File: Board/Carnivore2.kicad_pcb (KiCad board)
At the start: 2 copper layers, 99 x 65.6 mm, 135 parts, among them J1 Conn_01x02_Pin, J2 Conn_01x03_Pin, U1 EP2C8Q208C8N, U2 MX29LV640ETTI-70G, U3 RMLV1616AGSA-5S#KA0, U4 M25P80-VMN3TPB, U5 PCM5101APWR, U6 AT93C46DN-SH-T, U7 SG3225CAN 50.0000M-TJGA6, U9 PCM1808PWR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

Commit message: Corrections in silkscreen for wrong direction of some capacitors and all diodes
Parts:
- moved D4 7.66 mm to (188.4, 113.4), turned to 180 degrees
- moved D1 7.63 mm to (191.6, 82.2), turned to 180 degrees
- moved D2 7.60 mm to (191.7, 86.8), turned to -90 degrees
- moved D3 7.59 mm to (178.0, 113.4), turned to 180 degrees
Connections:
- D1 pad 1: /VCC3.3 -> Net-(D1-K)
- D1 pad 2: Net-(D1-K) -> /VCC3.3
- D2 pad 1: Net-(D2-A) -> Net-(D1-K)
- D2 pad 2: Net-(D1-K) -> Net-(D2-A)
- D3 pad 1: /VCC3.3 -> Net-(D3-K)
- D3 pad 2: Net-(D3-K) -> /VCC3.3
- D4 pad 1: Net-(D3-K) -> Net-(D4-K)
- D4 pad 2: Net-(D4-K) -> Net-(D3-K)
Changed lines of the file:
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@@
   )
   (footprint "Diode_THT:D_DO-35_SOD27_P7.62mm_Horizontal" (layer "F.Cu")
-    (at 183.98 82.22)
+    (at 191.61 82.22 180)
     (descr "Diode, DO-35_SOD27 series, Axial, Horizontal, pin pitch=7.62mm, , length*diameter=4*2mm^2, , http://www.diodes.com/_files/packages/DO-35.pdf")
     (tags "Diode DO-35_SOD27 series Axial Horizontal pin pitch 7.62mm  length 4mm diameter 2mm")
@@
     (property "Sheetfile" "Carnivore2.kicad_sch")
     (property "Sheetname" "")
-    (property "ki_description" "Default Diode")
+    (property "Sim.Device" "D")
+    (property "Sim.Pins" "1=K 2=A")
+    (property "ki_description" "100V 0.15A standard switching diode, DO-35")
+    (property "ki_keywords" "diode")
     (attr through_hole)
     (fp_text reference "D1" (at 4.07 0) (layer "F.SilkS")
@@
     (fp_line (start 7.62 0) (end 5.81 0)
       (stroke (width 0.1) (type solid)) (layer "F.Fab"))
-    (pad "1" thru_hole rect (at 0 0) (size 1.6 1.6) (drill 0.8) (layers "*.Cu" "*.Mask")
-      (net 4 "/VCC3.3") (pinfunction "A") (pintype "passive"))
-    (pad "2" thru_hole oval (at 7.62 0) (size 1.6 1.6) (drill 0.8) (layers "*.Cu" "*.Mask")
+    (pad "1" thru_hole rect (at 0 0 180) (size 1.6 1.6) (drill 0.8) (layers "*.Cu" "*.Mask")
       (net 7 "Net-(D1-K)") (pinfunction "K") (pintype "passive"))
+    (pad "2" thru_hole oval (at 7.62 0 180) (size 1.6 1.6) (drill 0.8) (layers "*.Cu" "*.Mask")
+      (net 4 "/VCC3.3") (pinfunction "A") (pintype "passive"))
     (model "${KICAD6_3DMODEL_DIR}/Diode_THT.3dshapes/D_DO-35_SOD27_P7.62mm_Horizontal.wrl"
       (offset (xyz 0 0 0))
@@
   )
   (footprint "Diode_THT:D_DO-35_SOD27_P7.62mm_Horizontal" (layer "F.Cu")
-    (at 191.65 94.37 90)
+    (at 191.65 86.77 -90)
     (descr "Diode, DO-35_SOD27 series, Axial, Horizontal, pin pitch=7.62mm, , length*diameter=4*2mm^2, , http://www.diodes.com/_files/packages/DO-35.pdf")
     (tags "Diode DO-35_SOD27 series Axial Horizontal pin pitch 7.62mm  length 4mm diameter 2mm")
@@
     (property "Sheetfile" "Carnivore2.kicad_sch")
     (property "Sheetname" "")
-    (property "ki_description" "Default Diode")
+    (property "Sim.Device" "D")
+    (property "Sim.Pins" "1=K 2=A")
+    (property "ki_description" "100V 0.15A standard switching diode, DO-35")
+    (property "ki_keywords" "diode")
     (attr through_hole)
     (fp_text reference "D2" (at 3.95 0.05 90) (layer "F.SilkS")
@@
     (fp_line (start 7.62 0) (end 5.81 0)
       (stroke (width 0.1) (type solid)) (layer "F.Fab"))
-    (pad "1" thru_hole rect (at 0 0 90) (size 1.6 1.6) (drill 0.8) (layers "*.Cu" "*.Mask")
-      (net 11 "Net-(D2-A)") (pinfunction "A") (pintype "passive"))
-    (pad "2" thru_hole oval (at 7.62 0 90) (size 1.6 1.6) (drill 0.8) (layers "*.Cu" "*.Mask")
+    (pad "1" thru_hole rect (at 0 0 270) (size 1.6 1.6) (drill 0.8) (layers "*.Cu" "*.Mask")
       (net 7 "Net-(D1-K)") (pinfunction "K") (pintype "passive"))
+    (pad "2" thru_hole oval (at 7.62 0 270) (size 1.6 1.6) (drill 0.8) (layers "*.Cu" "*.Mask")
+      (net 11 "Net-(D2-A)") (pinfunction "A") (pintype "passive"))
     (model "${KICAD6_3DMODEL_DIR}/Diode_THT.3dshapes/D_DO-35_SOD27_P7.62mm_Horizontal.wrl"
       (offset (xyz 0 0 0))
@@
   )
   (footprint "Diode_THT:D_DO-35_SOD27_P7.62mm_Horizontal" (layer "F.Cu")
-    (at 180.78 113.38)
+    (at 188.44 113.37 180)
     (descr "Diode, DO-35_SOD27 series, Axial, Horizontal, pin pitch=7.62mm, , length*diameter=4*2mm^2, , http://www.diodes.com/_files/packages/DO-35.pdf")
     (tags "Diode DO-35_SOD27 series Axial Horizontal pin pitch 7.62mm  length 4mm diameter 2mm")
@@
     (property "Sheetfile" "Carnivore2.kicad_sch")
     (property "Sheetname" "")
-    (property "ki_description" "Default Diode")
+    (property "Sim.Device" "D")
+    (property "Sim.Pins" "1=K 2=A")
+    (property "ki_description" "100V 0.15A standard switching diode, DO-35")
+    (property "ki_keywords" "diode")
     (attr through_hole)
-    (fp_text reference "D4" (at 3.81 -2.12) (layer "F.SilkS")
+    (fp_text reference "D4" (at 3.32 1.93) (layer "F.SilkS")
         (effects (font (size 1 1) (thickness 0.15)))
     )
@@
     (fp_line (start 7.62 0) (end 5.81 0)
       (stroke (width 0.1) (type solid)) (layer "F.Fab"))
-    (pad "1" thru_hole rect (at 0 0) (size 1.6 1.6) (drill 0.8) (layers "*.Cu" "*.Mask")
-      (net 12 "Net-(D3-K)") (pinfunction "A") (pintype "passive"))
-    (pad "2" thru_hole oval (at 7.62 0) (size 1.6 1.6) (drill 0.8) (layers "*.Cu" "*.Mask")
+    (pad "1" thru_hole rect (at 0 0 180) (size 1.6 1.6) (drill 0.8) (layers "*.Cu" "*.Mask")
       (net 13 "Net-(D4-K)") (pinfunction "K") (pintype "passive"))
+    (pad "2" thru_hole oval (at 7.62 0 180) (size 1.6 1.6) (drill 0.8) (layers "*.Cu" "*.Mask")
+      (net 12 "Net-(D3-K)") (pinfunction "A") (pintype "passive"))
     (model "${KICAD6_3DMODEL_DIR}/Diode_THT.3dshapes/D_DO-35_SOD27_P7.62mm_Horizontal.wrl"
       (offset (xyz 0 0 0))
@@
   )
   (footprint "Diode_THT:D_DO-35_SOD27_P7.62mm_Horizontal" (layer "F.Cu")
-    (at 170.44 113.37)
+    (at 178.03 113.41 180)
     (descr "Diode, DO-35_SOD27 series, Axial, Horizontal, pin pitch=7.62mm, , length*diameter=4*2mm^2, , http://www.diodes.com/_files/packages/DO-35.pdf")
     (tags "Diode DO-35_SOD27 series Axial Horizontal pin pitch 7.62mm  length 4mm diameter 2mm")
@@
     (property "Sheetfile" "Carnivore2.kicad_sch")
     (property "Sheetname" "")
-    (property "ki_description" "Default Diode")
+    (property "Sim.Device" "D")
+    (property "Sim.Pins" "1=K 2=A")
+    (property "ki_description" "100V 0.15A standard switching diode, DO-35")
+    (property "ki_keywords" "diode")
     (attr through_hole)
-    (fp_text reference "D3" (at 3.81 -2.12) (layer "F.SilkS")
+    (fp_text reference "D3" (at 3.5 1.95) (layer "F.SilkS")
         (effects (font (size 1 1) (thickness 0.15)))
     )
@@
     (fp_line (start 7.62 0) (end 5.81 0)
       (stroke (width 0.1) (type solid)) (layer "F.Fab"))
-    (pad "1" thru_hole rect (at 0 0) (size 1.6 1.6) (drill 0.8) (layers "*.Cu" "*.Mask")
-      (net 4 "/VCC3.3") (pinfunction "A") (pintype "passive"))
-    (pad "2" thru_hole oval (at 7.62 0) (size 1.6 1.6) (drill 0.8) (layers "*.Cu" "*.Mask")
+    (pad "1" thru_hole rect (at 0 0 180) (size 1.6 1.6) (drill 0.8) (layers "*.Cu" "*.Mask")
       (net 12 "Net-(D3-K)") (pinfunction "K") (pintype "passive"))
+    (pad "2" thru_hole oval (at 7.62 0 180) (size 1.6 1.6) (drill 0.8) (layers "*.Cu" "*.Mask")
+      (net 4 "/VCC3.3") (pinfunction "A") (pintype "passive"))
     (model "${KICAD6_3DMODEL_DIR}/Diode_THT.3dshapes/D_DO-35_SOD27_P7.62mm_Horizontal.wrl"
       (offset (xyz 0 0 0))
@@
     (effects (font (size 1.01024 1.0626) (thickness 0.154)))
   )
-  (gr_text "+" (at 110.15 112.31) (layer "F.SilkS")
+  (gr_text "+" (at 116.29 111.89) (layer "F.SilkS")
     (effects (font (size 1.01024 1.0626) (thickness 0.154)))
   )
@@
     (effects (font (size 1.01024 1.0626) (thickness 0.154)))
   )
-  (gr_text "+" (at 118.66 93.17) (layer "F.SilkS")
+  (gr_text "+" (at 118.72 86.94) (layer "F.SilkS")
     (effects (font (size 1.01024 1.0626) (thickness 0.154)))
   )

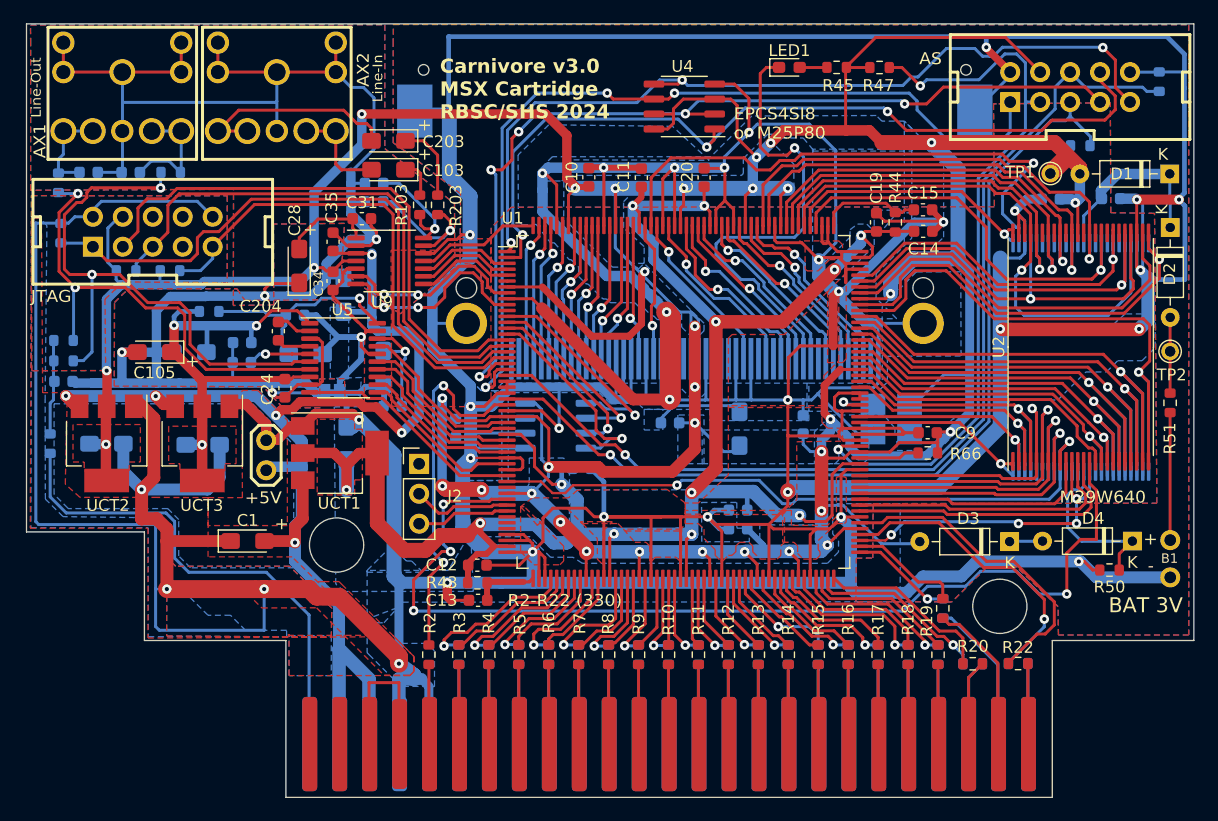
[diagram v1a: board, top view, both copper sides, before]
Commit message: Hardware modification to delay Z80 startup until FPGA is configured Needed on FS-A1W(S)X models
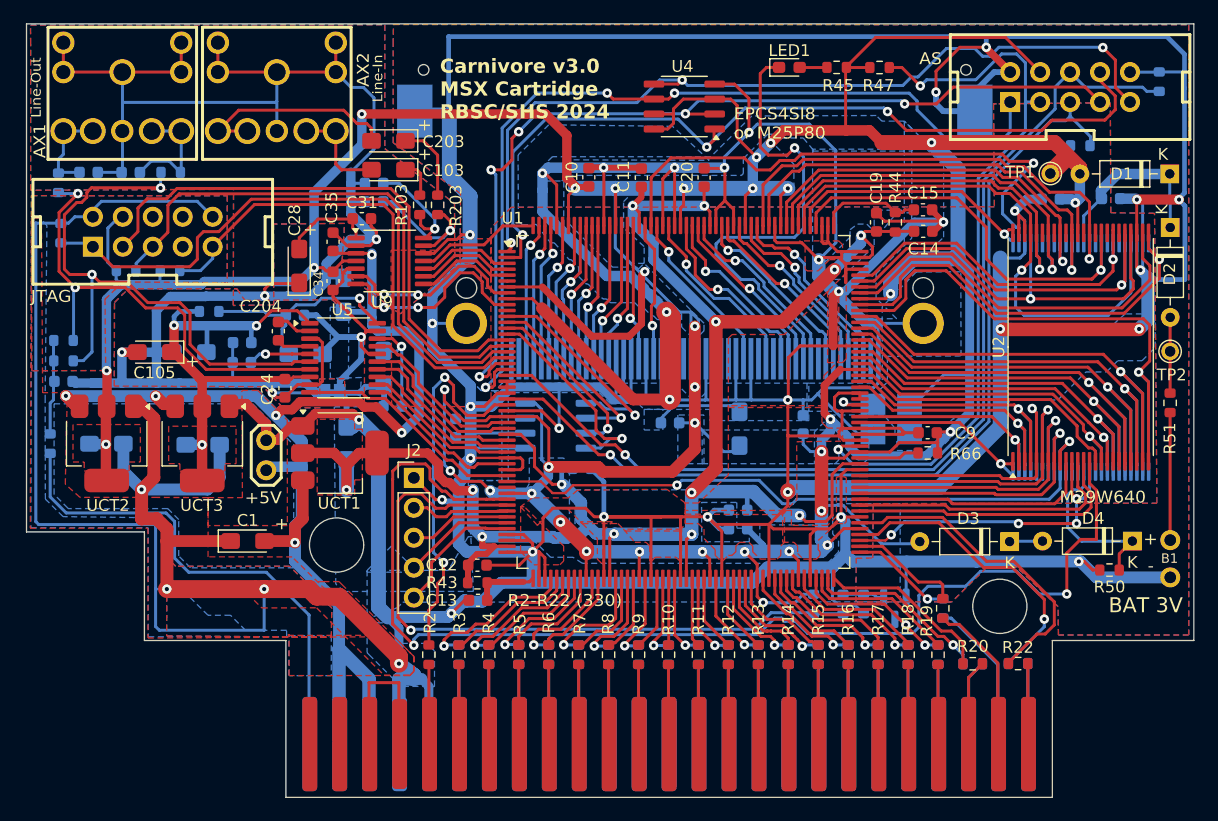
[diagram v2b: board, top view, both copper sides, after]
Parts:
- added Q1: MMBT3904-TP, Package_TO_SOT_SMD:SOT-23, B.Cu at (168.3, 119.1)
- added R52: 10k, Resistor_SMD:R_0603_1608Metric, B.Cu at (165.6, 118.7)
- added R53: 4k7, Resistor_SMD:R_0603_1608Metric, B.Cu at (161.4, 118.7)
- added R54: 4k7, Resistor_SMD:R_0603_1608Metric, B.Cu at (163.9, 118.7)
- J2: value Conn_01x03_Pin -> Conn_01x05_Pin; footprint Connector_PinHeader_2.54mm:PinHeader_1x03_P2.54mm_Vertical -> Connector_PinHeader_2.54mm:PinHeader_1x05_P2.54mm_Vertical
- X2, X3: value 302-S101 -> HEADER_5X2
- moved J2 1.27 mm to (127.5, 108.0)
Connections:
- U1 pad 44: Net-(J2-Pin_2) -> /~{SLT_READY}
- U1 pad 45: Net-(J2-Pin_3) -> Net-(J2-Pin_2)
- U1 pad 46: unconnected-(U1A-IO-Pad46) -> Net-(J2-Pin_3)
- U1 pad 47: unconnected-(U1A-IO,_PLL1_OUTp-Pad47) -> Net-(J2-Pin_4)
- U1 pad 48: unconnected-(U1A-IO,_PLL1_OUTn-Pad48) -> Net-(J2-Pin_5)
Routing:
- net /~{SLT_READY}: track 0.00 -> 59.0 mm, vias 0 -> 1
- net /GND: track 1031.2 -> 1054.9 mm, vias 35 -> 38
- net /RVPPE: track 87.3 -> 102.0 mm, vias 4 -> 2
- net Net-(J2-Pin_5): track 0.00 -> 11.2 mm
- net Net-(J2-Pin_4): track 0.00 -> 10.2 mm
- net /VCC3.3: track 473.3 -> 478.9 mm, vias 34 -> 35
- net /VCC1.2: track 166.7 -> 163.1 mm, vias 12 -> 13
- net Net-(Q1-B): track 0.00 -> 3.55 mm
- net /~{SLT_WAIT}: track 13.6 -> 14.8 mm, vias 1 -> 2
- net /SLT_CLC: track 30.9 -> 31.8 mm
- net /RSW1: track 8.58 -> 9.31 mm
- net Net-(J2-Pin_3): track 7.94 -> 8.64 mm
- net /TCK: track 53.1 -> 53.8 mm
- net /SLT_A15: track 7.72 -> 8.36 mm
- net /~{SLT_M1}: track 13.6 -> 13.0 mm
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
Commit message: Minor improvements
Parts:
- X2, X3: value HEADER_5X2 -> 302-S101
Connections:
- net /VCC1.2 renamed /+1V2
- net /VCC3.3 renamed /+3.3V
- net /VCC3.3A renamed /+3.3VDAC
- net /VCC5 renamed /+5V

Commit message: Improved slot wait
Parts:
- R54: value 4k7 -> 470E
- moved R21 0.30 mm to (172.5, 118.8)
- moved R24 0.27 mm to (172.5, 118.8)
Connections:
- Q1 pad 3: /~{SLT_WAIT} -> /~{X_SLT_WAIT}
- R26 pad 2: Net-(R26-Pad2) -> /~{X_SLT_WAIT}
- X1 pad 7: Net-(R26-Pad2) -> /~{X_SLT_WAIT}
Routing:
- net /~{X_SLT_WAIT}: track 0.00 -> 14.0 mm, vias 0 -> 2
- net Net-(R26-Pad2): track 5.82 -> 0.00 mm
- net /+3.3V: track 478.9 -> 481.8 mm
- net /~{SLT_WAIT}: track 14.8 -> 13.6 mm, vias 2 -> 1
